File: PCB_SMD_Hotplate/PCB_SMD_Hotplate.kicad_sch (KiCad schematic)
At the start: 65 parts, among them J1 CONN_POWER, J10 CONN_DIFF_01, J11 CONN_DIFF_02, J12 CONN_HEADER, J2 USB_C_16P, J3 CONN_ADC, J4 CONN_OLED, J5 CONN_FAN, J6 CONN_LED, J7 CONN_ENCODER, J8 CONN_SSR, J9 CONN_ICSP, Q1 2N7002, SW1 SW_Push, U1 LM7805_TO220, U2 CH340C, U3 ICL7660, U4 LM324, U5 ATmega328P-A, Y1 16MHz

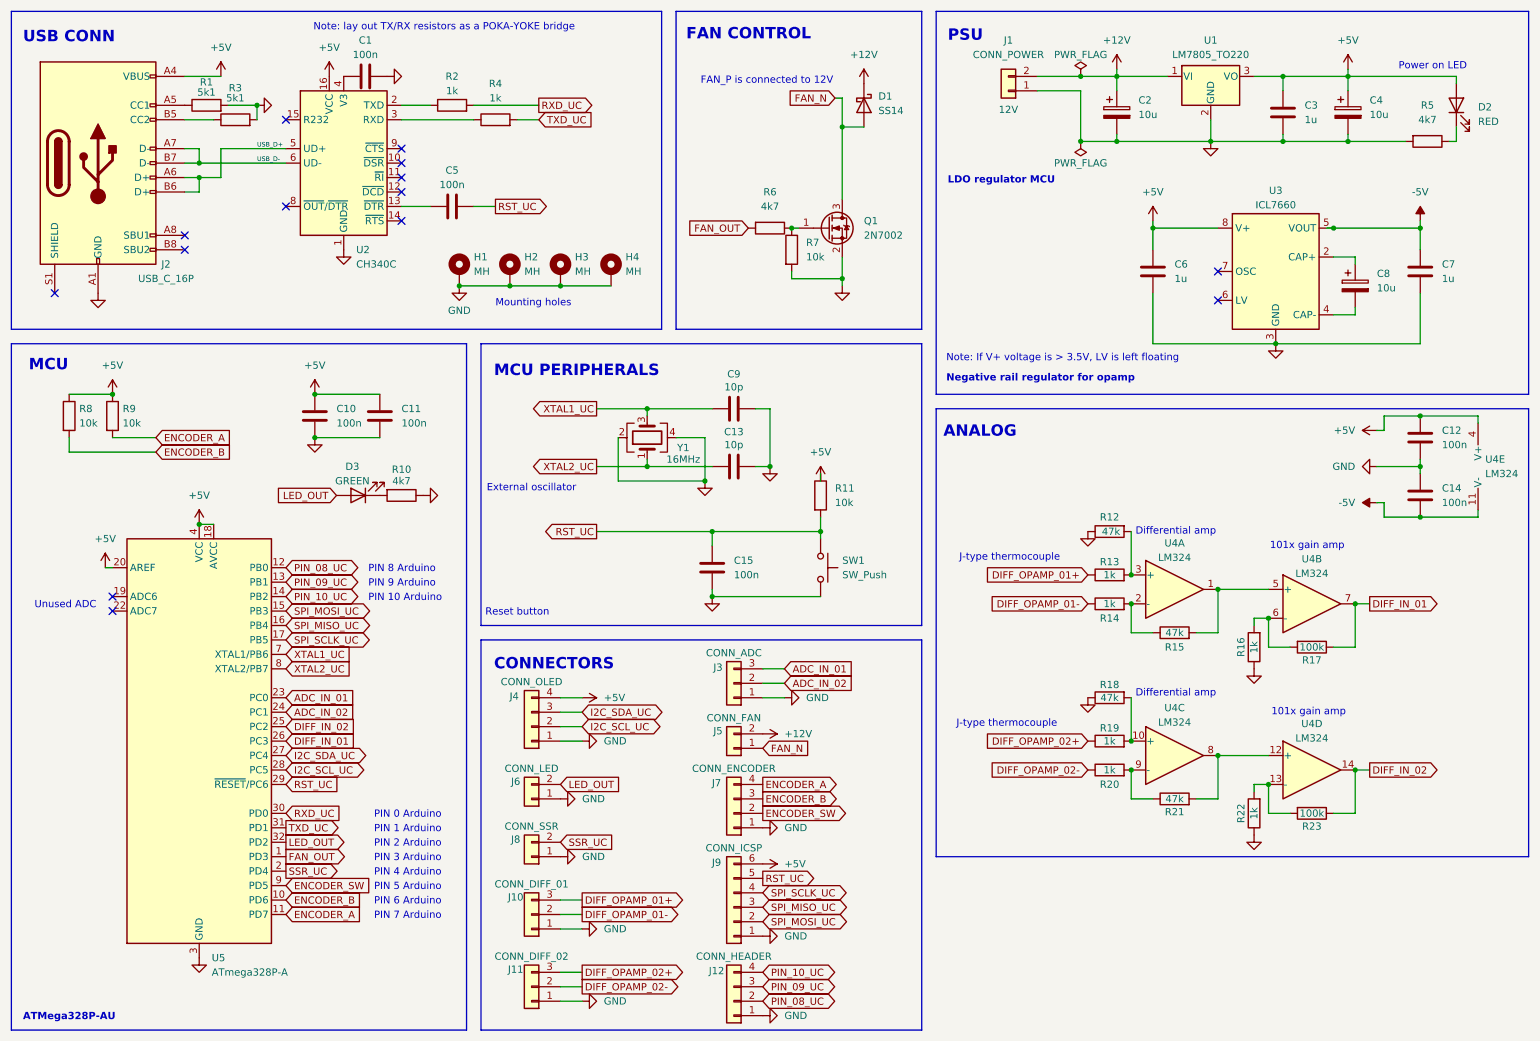
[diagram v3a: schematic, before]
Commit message: Finish PCB and prepare files for ordering
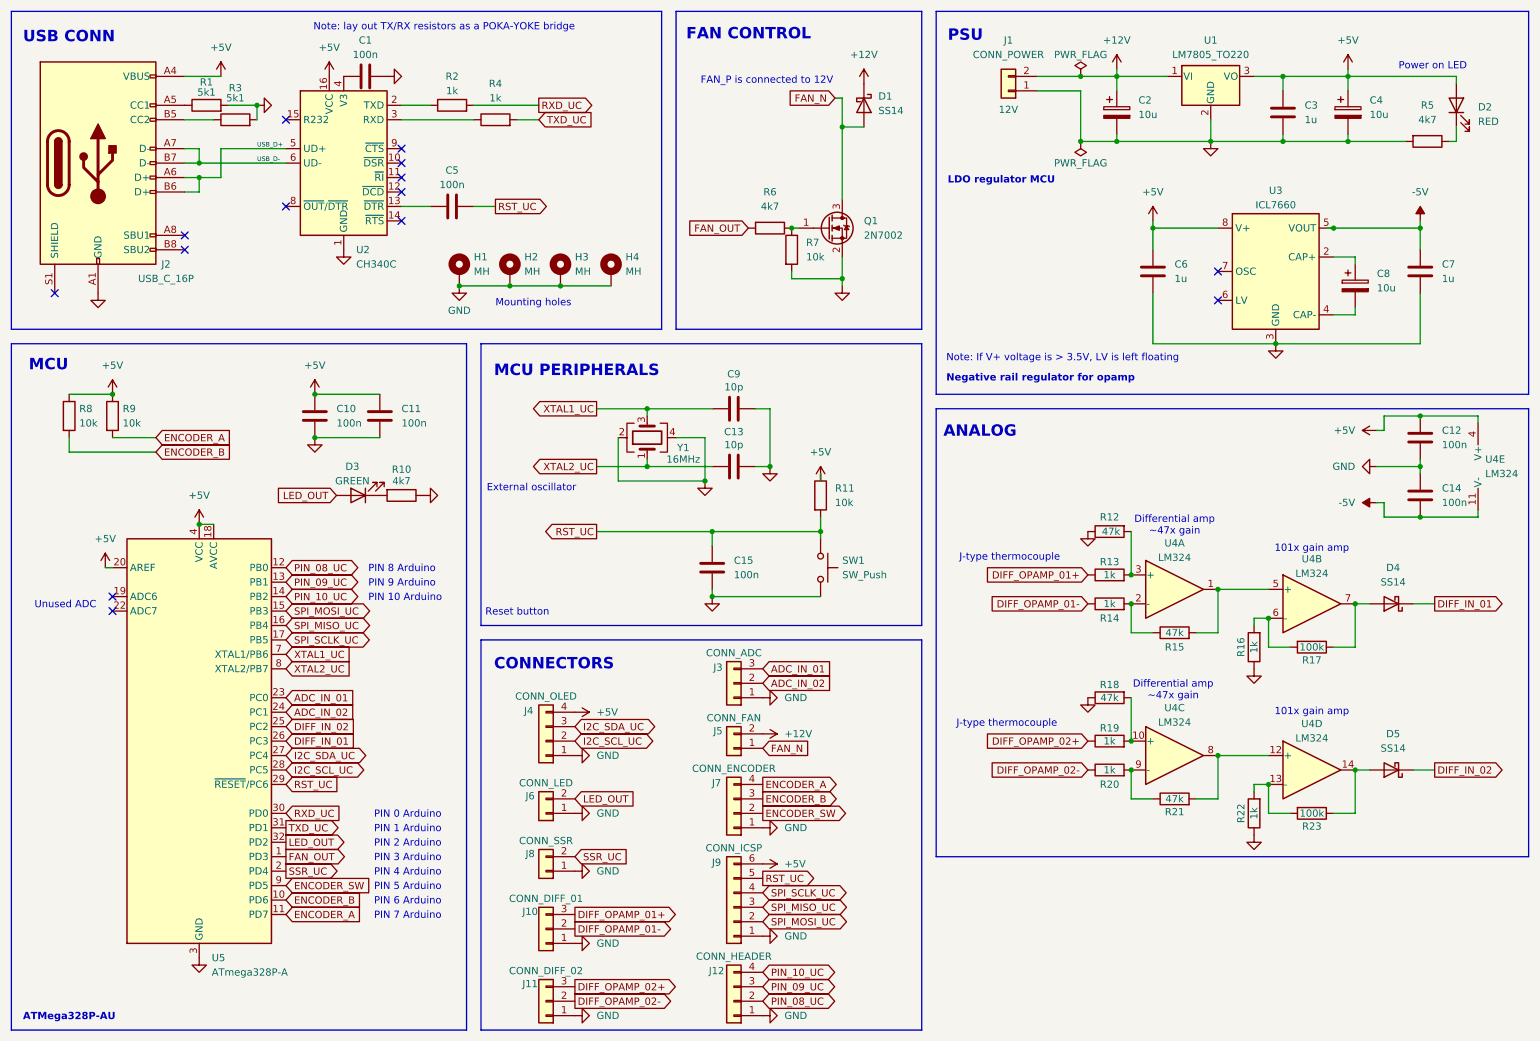
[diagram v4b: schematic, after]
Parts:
- added D4, D5: SS14, Diode_SMD:D_SMA, symbol Diode:SS14
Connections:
- net DIFF_IN_01: now also D4.1 (K); no longer R17.1, U4.7
- net DIFF_IN_02: now also D5.1 (K); no longer R23.1, U4.14
- new net: D5.2 (A), R23.1, U4.14
- new net: D4.2 (A), R17.1, U4.7
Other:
- note added: "Differential amp ~47x gain"
- note removed: "Differential amp"
- company: (none) -> Aleksa Heler
- title: (none) -> SMD Hotplate Controller
- moved on the sheet: J10, J11, J4, J6, J8
